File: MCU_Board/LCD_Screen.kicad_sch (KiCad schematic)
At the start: 2 parts

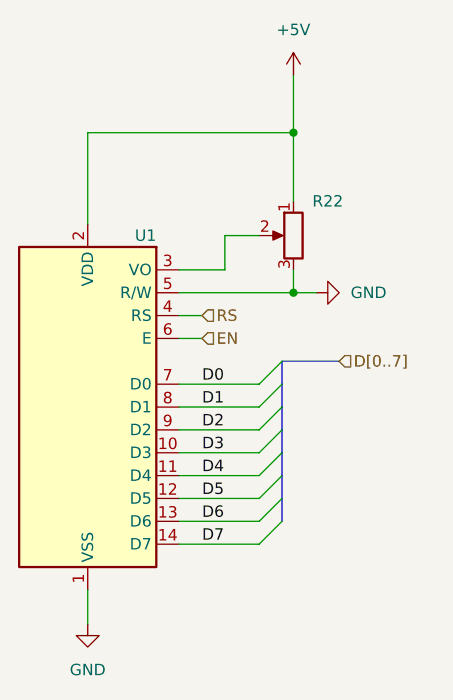
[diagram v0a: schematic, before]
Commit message: Finished MCU board
Finished MCU board and started finishing up the VCO board
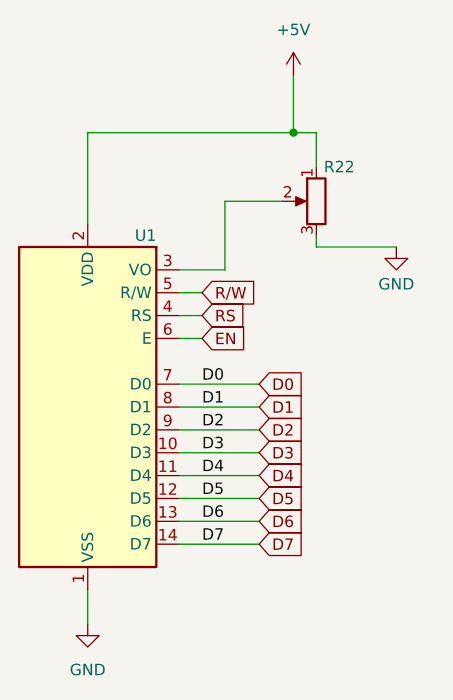
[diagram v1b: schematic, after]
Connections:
- net GND: no longer U1.5 (R/W)
- new net R/W: U1.5 (R/W)
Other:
- moved on the sheet: R22
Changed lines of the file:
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@@
   (junction (at 143.51 62.23) (diameter 0) (color 0 0 0 0)
   )
-  (junction (at 143.51 80.01) (diameter 0) (color 0 0 0 0)
-  )
-  (bus_entry (at 139.7 102.87) (size 2.54 -2.54)
-    (stroke (width 0) (type default))
-  )
-  (bus_entry (at 139.7 107.95) (size 2.54 -2.54)
-    (stroke (width 0) (type default))
-  )
-  (bus_entry (at 139.7 92.71) (size 2.54 -2.54)
-    (stroke (width 0) (type default))
-  )
-  (bus_entry (at 139.7 97.79) (size 2.54 -2.54)
-    (stroke (width 0) (type default))
-  )
-  (bus_entry (at 139.7 90.17) (size 2.54 -2.54)
-    (stroke (width 0) (type default))
-  )
-  (bus_entry (at 139.7 105.41) (size 2.54 -2.54)
-    (stroke (width 0) (type default))
-  )
-  (bus_entry (at 139.7 95.25) (size 2.54 -2.54)
-    (stroke (width 0) (type default))
-  )
-  (bus_entry (at 139.7 100.33) (size 2.54 -2.54)
-    (stroke (width 0) (type default))
-  )
-  (bus (pts (xy 142.24 95.25) (xy 142.24 97.79))
-    (stroke (width 0) (type default))
-  )
-  (bus (pts (xy 142.24 97.79) (xy 142.24 100.33))
-    (stroke (width 0) (type default))
-  )
-  (bus (pts (xy 142.24 87.63) (xy 142.24 90.17))
-    (stroke (width 0) (type default))
-  )
-  (bus (pts (xy 142.24 90.17) (xy 142.24 92.71))
-    (stroke (width 0) (type default))
-  )
   (wire (pts (xy 130.81 90.17) (xy 139.7 90.17))
     (stroke (width 0) (type default))
   )
-  (wire (pts (xy 139.7 73.66) (xy 135.89 73.66))
+  (wire (pts (xy 142.24 69.85) (xy 135.89 69.85))
     (stroke (width 0) (type default))
   )
@@
     (stroke (width 0) (type default))
   )
-  (wire (pts (xy 135.89 73.66) (xy 135.89 77.47))
-    (stroke (width 0) (type default))
-  )
-  (bus (pts (xy 148.59 87.63) (xy 142.24 87.63))
-    (stroke (width 0) (type default))
-  )
-  (bus (pts (xy 142.24 100.33) (xy 142.24 102.87))
+  (wire (pts (xy 135.89 69.85) (xy 135.89 77.47))
     (stroke (width 0) (type default))
   )
@@
     (stroke (width 0) (type default))
   )
+  (wire (pts (xy 154.94 74.93) (xy 146.05 74.93))
+    (stroke (width 0) (type default))
+  )
   (wire (pts (xy 130.81 97.79) (xy 139.7 97.79))
     (stroke (width 0) (type default))
@@
     (stroke (width 0) (type default))
   )
-  (wire (pts (xy 130.81 80.01) (xy 143.51 80.01))
-    (stroke (width 0) (type default))
-  )
   (wire (pts (xy 130.81 102.87) (xy 139.7 102.87))
     (stroke (width 0) (type default))
@@
     (stroke (width 0) (type default))
   )
-  (bus (pts (xy 142.24 92.71) (xy 142.24 95.25))
+  (wire (pts (xy 146.05 62.23) (xy 143.51 62.23))
     (stroke (width 0) (type default))
   )
@@
     (stroke (width 0) (type default))
   )
-  (wire (pts (xy 143.51 62.23) (xy 143.51 69.85))
+  (wire (pts (xy 146.05 74.93) (xy 146.05 73.66))
+    (stroke (width 0) (type default))
+  )
+  (wire (pts (xy 146.05 62.23) (xy 146.05 66.04))
     (stroke (width 0) (type default))
   )
@@
     (stroke (width 0) (type default))
   )
-  (bus (pts (xy 142.24 102.87) (xy 142.24 105.41))
-    (stroke (width 0) (type default))
-  )
   (wire (pts (xy 130.81 100.33) (xy 139.7 100.33))
     (stroke (width 0) (type default))
   )
-  (wire (pts (xy 143.51 80.01) (xy 146.05 80.01))
-    (stroke (width 0) (type default))
-  )
   (wire (pts (xy 120.65 62.23) (xy 143.51 62.23))
     (stroke (width 0) (type default))
   )
-  (wire (pts (xy 143.51 77.47) (xy 143.51 80.01))
+  (wire (pts (xy 130.81 80.01) (xy 133.35 80.01))
     (stroke (width 0) (type default))
   )
@@
     (effects (font (size 1.27 1.27)) (justify left bottom))
   )
-  (hierarchical_label "D[0..7]" (shape input) (at 148.59 87.63 0) (fields_autoplaced)
-    (effects (font (size 1.27 1.27)) (justify left))
-  )
-  (hierarchical_label "RS" (shape input) (at 133.35 82.55 0) (fields_autoplaced)
-    (effects (font (size 1.27 1.27)) (justify left))
-  )
-  (hierarchical_label "EN" (shape input) (at 133.35 85.09 0) (fields_autoplaced)
-    (effects (font (size 1.27 1.27)) (justify left))
+  (global_label "D0" (shape input) (at 139.7 90.17 0) (fields_autoplaced)
+    (effects (font (size 1.27 1.27)) (justify left))
+    (property "Intersheetrefs" "${INTERSHEET_REFS}" (at 144.5105 90.17 0)
+      (effects (font (size 1.27 1.27)) (justify left) hide)
+    )
+  )
+  (global_label "EN" (shape input) (at 133.35 85.09 0) (fields_autoplaced)
+    (effects (font (size 1.27 1.27)) (justify left))
+    (property "Intersheetrefs" "${INTERSHEET_REFS}" (at 138.1605 85.09 0)
+      (effects (font (size 1.27 1.27)) (justify left) hide)
+    )
+  )
+  (global_label "D2" (shape input) (at 139.7 95.25 0) (fields_autoplaced)
+    (effects (font (size 1.27 1.27)) (justify left))
+    (property "Intersheetrefs" "${INTERSHEET_REFS}" (at 144.5105 95.25 0)
+      (effects (font (size 1.27 1.27)) (justify left) hide)
+    )
+  )
+  (global_label "D5" (shape input) (at 139.7 102.87 0) (fields_autoplaced)
+    (effects (font (size 1.27 1.27)) (justify left))
+    (property "Intersheetrefs" "${INTERSHEET_REFS}" (at 144.5105 102.87 0)
+      (effects (font (size 1.27 1.27)) (justify left) hide)
+    )
+  )
+  (global_label "RS" (shape input) (at 133.35 82.55 0) (fields_autoplaced)
+    (effects (font (size 1.27 1.27)) (justify left))
+    (property "Intersheetrefs" "${INTERSHEET_REFS}" (at 138.1605 82.55 0)
+      (effects (font (size 1.27 1.27)) (justify left) hide)
+    )
+  )
+  (global_label "D4" (shape input) (at 139.7 100.33 0) (fields_autoplaced)
+    (effects (font (size 1.27 1.27)) (justify left))
+    (property "Intersheetrefs" "${INTERSHEET_REFS}" (at 144.5105 100.33 0)
+      (effects (font (size 1.27 1.27)) (justify left) hide)
+    )
+  )
+  (global_label "D7" (shape input) (at 139.7 107.95 0) (fields_autoplaced)
+    (effects (font (size 1.27 1.27)) (justify left))
+    (property "Intersheetrefs" "${INTERSHEET_REFS}" (at 144.5105 107.95 0)
+      (effects (font (size 1.27 1.27)) (justify left) hide)
+    )
+  )
+  (global_label "D3" (shape input) (at 139.7 97.79 0) (fields_autoplaced)
+    (effects (font (size 1.27 1.27)) (justify left))
+    (property "Intersheetrefs" "${INTERSHEET_REFS}" (at 144.5105 97.79 0)
+      (effects (font (size 1.27 1.27)) (justify left) hide)
+    )
+  )
+  (global_label "D1" (shape input) (at 139.7 92.71 0) (fields_autoplaced)
+    (effects (font (size 1.27 1.27)) (justify left))
+    (property "Intersheetrefs" "${INTERSHEET_REFS}" (at 144.5105 92.71 0)
+      (effects (font (size 1.27 1.27)) (justify left) hide)
+    )
+  )
+  (global_label "R{slash}W" (shape input) (at 133.35 80.01 0) (fields_autoplaced)
+    (effects (font (size 1.27 1.27)) (justify left))
+    (property "Intersheetrefs" "${INTERSHEET_REFS}" (at 139.7329 80.01 0)
+      (effects (font (size 1.27 1.27)) (justify left) hide)
+    )
+  )
+  (global_label "D6" (shape input) (at 139.7 105.41 0) (fields_autoplaced)
+    (effects (font (size 1.27 1.27)) (justify left))
+    (property "Intersheetrefs" "${INTERSHEET_REFS}" (at 144.5105 105.41 0)
+      (effects (font (size 1.27 1.27)) (justify left) hide)
+    )
   )
   (symbol (lib_id "ADF_5355_Lib:LCD_16x2") (at 120.65 93.98 0) (mirror y) (unit 1)
@@
     )
   )
-  (symbol (lib_id "power:GND") (at 146.05 80.01 90) (unit 1)
+  (symbol (lib_id "power:GND") (at 154.94 74.93 0) (unit 1)
     (in_bom yes) (on_board yes) (dnp no) (fields_autoplaced)
-    (property "Reference" "#PWR025" (at 152.4 80.01 0)
-      (effects (font (size 1.27 1.27)) hide)
-    )
-    (property "Value" "GND" (at 149.86 80.01 90)
-      (effects (font (size 1.27 1.27)) (justify right))
-    )
-    (property "Footprint" "" (at 146.05 80.01 0)
-      (effects (font (size 1.27 1.27)) hide)
-    )
-    (property "Datasheet" "" (at 146.05 80.01 0)
+    (property "Reference" "#PWR025" (at 154.94 81.28 0)
+      (effects (font (size 1.27 1.27)) hide)
+    )
+    (property "Value" "GND" (at 154.94 79.0631 0)
+      (effects (font (size 1.27 1.27)))
+    )
+    (property "Footprint" "" (at 154.94 74.93 0)
+      (effects (font (size 1.27 1.27)) hide)
+    )
+    (property "Datasheet" "" (at 154.94 74.93 0)
       (effects (font (size 1.27 1.27)) hide)
     )
@@
     )
   )
-  (symbol (lib_id "Device:R_Potentiometer") (at 143.51 73.66 0) (mirror y) (unit 1)
+  (symbol (lib_id "Device:R_Potentiometer") (at 146.05 69.85 0) (mirror y) (unit 1)
     (in_bom yes) (on_board yes) (dnp no)
-    (property "Reference" "R22" (at 147.32 69.85 0)
-      (effects (font (size 1.27 1.27)))
-    )
-    (property "Value" "10k" (at 149.86 73.66 90)
-      (effects (font (size 1.27 1.27)) hide)
-    )
-    (property "Footprint" "Potentiometer_THT:Potentiometer_ACP_CA9-V10_Vertical" (at 143.51 73.66 0)
-      (effects (font (size 1.27 1.27)) hide)
-    )
-    (property "Datasheet" "~" (at 143.51 73.66 0)
-      (effects (font (size 1.27 1.27)) hide)
-    )
+    (property "Reference" "R22" (at 148.59 66.04 0)
+      (effects (font (size 1.27 1.27)))
+    )
+    (property "Value" "10k" (at 152.4 69.85 90)
+      (effects (font (size 1.27 1.27)) hide)
+    )
+    (property "Footprint" "Potentiometer_THT:Potentiometer_ACP_CA9-V10_Vertical" (at 146.05 69.85 0)
+      (effects (font (size 1.27 1.27)) hide)
+    )
+    (property "Datasheet" "~" (at 146.05 69.85 0)
+      (effects (font (size 1.27 1.27)) hide)
+    )
